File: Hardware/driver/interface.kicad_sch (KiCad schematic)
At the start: 45 parts, among them J201 Conn_02x10_Odd_Even, M201 Fan_4pin, Q201 MMBT3904, Q202 PN2222A, U201 AT24CS32-SSHM, U202 ADUM1250, U203 FODM214, U204 EMC2101-R, U205 NCP716BCSN330T1G

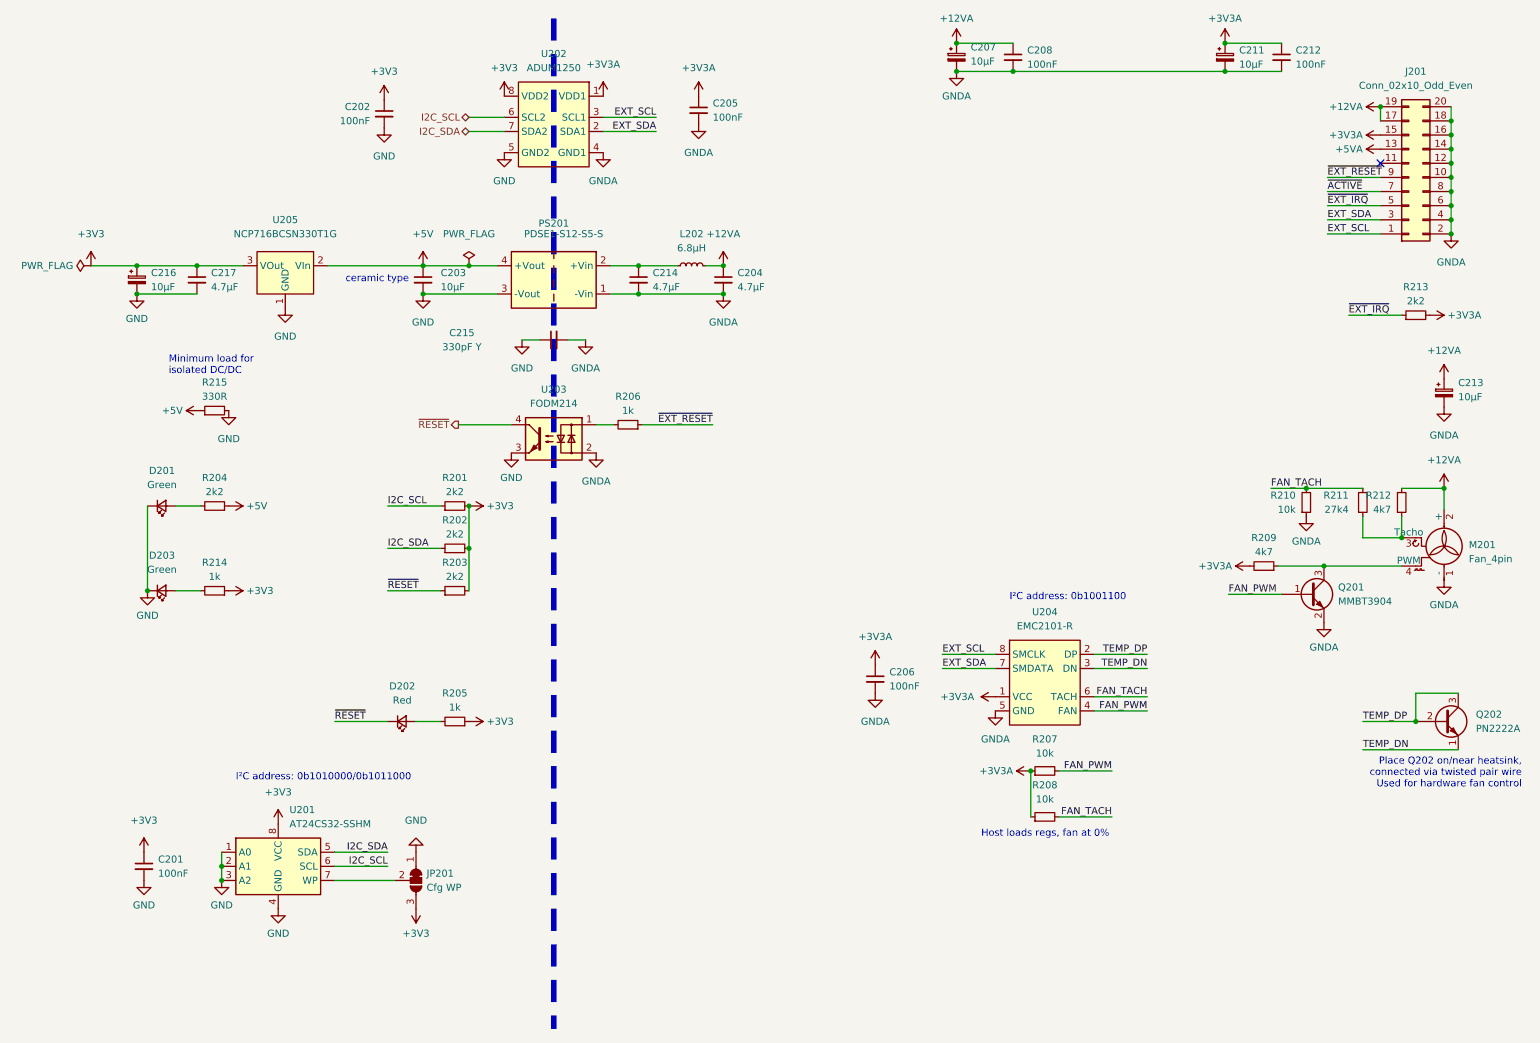
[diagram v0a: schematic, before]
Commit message: External trigger input
- Added a basic Schmitt-trigger based external trigger input. There's a
  basic pulse shaping circuit attached to it, before its fed into the
  buffer, and then off to the main board to use as an interrupt line to
  control the system mode.
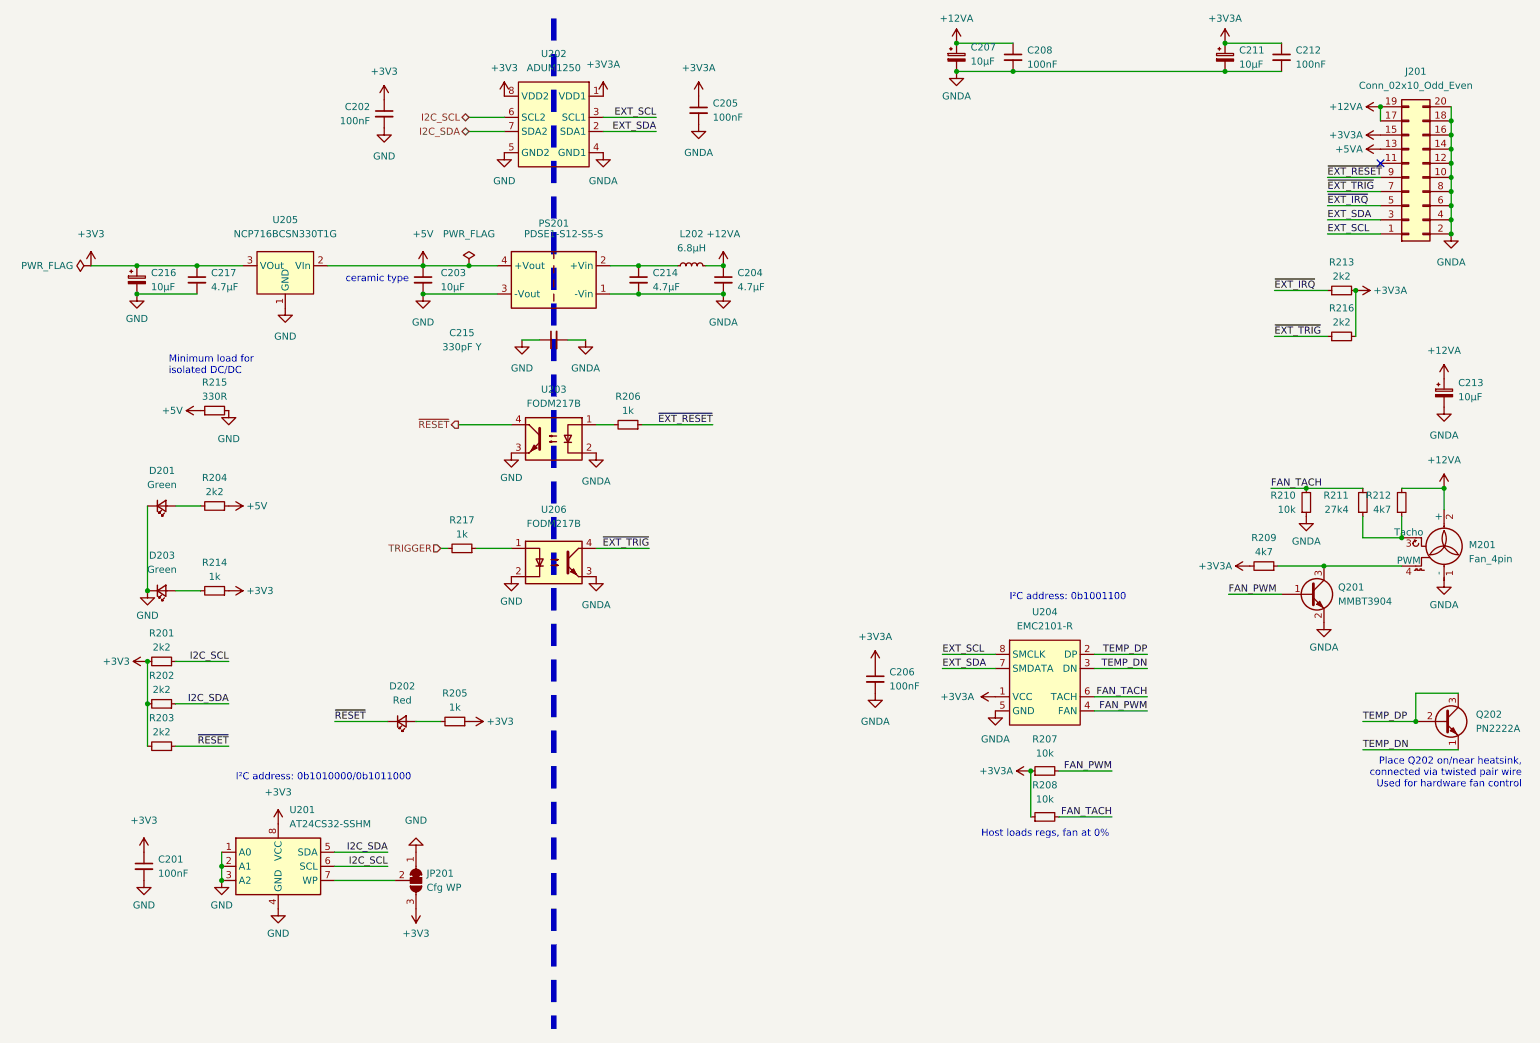
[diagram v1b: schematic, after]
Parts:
- added R216: 2k2, Resistor_SMD:R_0805_2012Metric_Pad1.20x1.40mm_HandSolder, symbol Device:R_Small
- added R217: 1k, Resistor_SMD:R_0805_2012Metric_Pad1.20x1.40mm_HandSolder, symbol Device:R_Small
- added U206: FODM217B, Package_SO:SOP-4_4.4x2.6mm_P1.27mm, symbol Isolator:FODM217B
- U203: value FODM214 -> FODM217B; symbol Isolator:FODM214 -> Isolator:FODM217B; MPN (none) -> FODM217B
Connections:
- net +3V3A: now also R216.2
- net GND: now also U206.2
- net GNDA: now also U206.3
- net ~{ACTIVE} renamed ~{EXT_TRIG}
- net ~{EXT_TRIG}: now also R216.1, U206.4
- new net: R217.1, U206.1
- new net TRIGGER: R217.2
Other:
- moved on the sheet: R201, R202, R203, R213

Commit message: Start work on remote VSense; driver board tweaks
- Use the DAC reference as the positive end of the null adjustment
  trimmers, rather than the +3V3 supply; this should make the adjustment
  actually useful and persistent rather than relying on the relationship
  between the 3V3 rail and the DAC's internal reference.

- Moved the 1Wire controller slightly to allow relocating the zero
  offset trimmer for the first channel

- Start work on remote VSense

  This works by selecting between either voltage sensing at the source
  terminals, or an external sense input connected to another set of
  terminals. These are switched by a latching relay (as to provide
  satisfying clicky noises) and then go into an op amp working as a
  differential amplifier; it performs a 50:1 gain (obviating the need
  for resistor dividers, and providing greater accuracy) and that then
  goes into the measurement ADC as normal.

  We have to still figure out how to drive the relay (probably just an
  IO expander?) and place those components on the board.
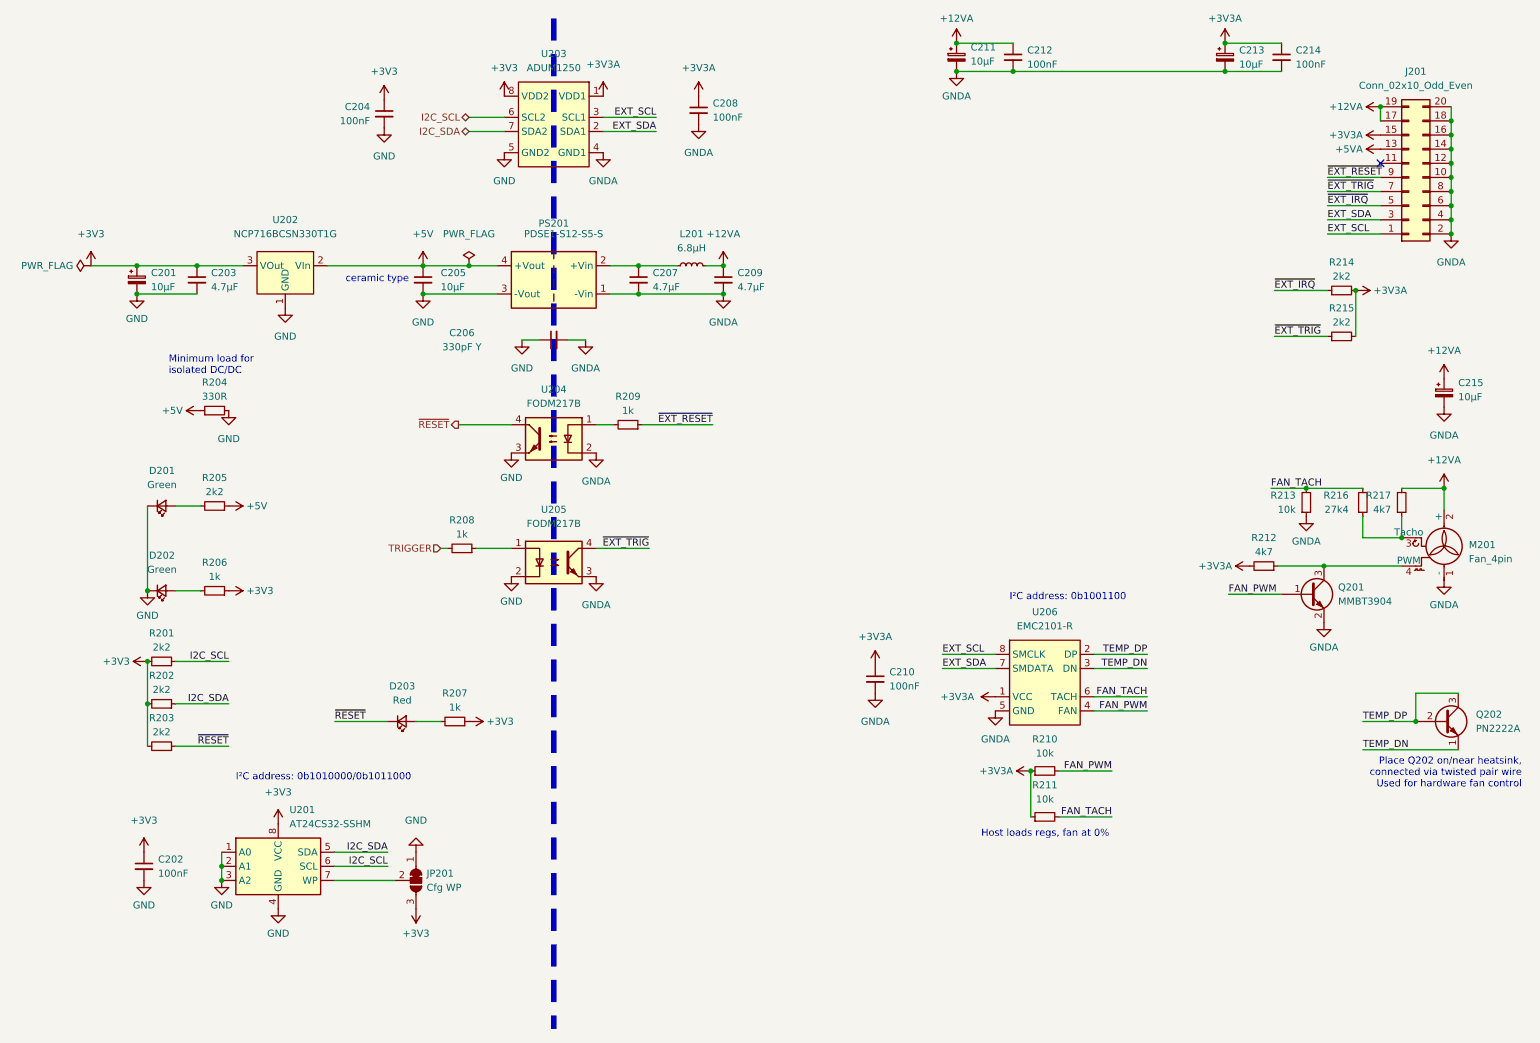
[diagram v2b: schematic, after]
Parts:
- renumbered C216 to C201, C201 to C202, C217 to C203, C202 to C204, C203 to C205, C215 to C206, C214 to C207, C205 to C208, C204 to C209, C206 to C210, C207 to C211, C208 to C212, C211 to C213, C212 to C214, C213 to C215, D203 to D202, D202 to D203, L202 to L201, R215 to R204, R204 to R205, R214 to R206, R205 to R207, R217 to R208, R206 to R209, R207 to R210, R208 to R211, R209 to R212, R210 to R213, R213 to R214, R216 to R215, R211 to R216, R212 to R217, U205 to U202, U202 to U203, U203 to U204, U206 to U205, U204 to U206

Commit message: Begin rev2 of driver board
- Improve the power side of things to provide +15V, +12V, +5V, +3V3, and
  -5V on the isolated side of the driver board. This is needed so that
  we can have the +12V for driving opamps with wider swing for the
  drive MOSFETs; these will not turn on with 3V3 as in the original rev1
  design so new driver op amps (U302, U306) need to be chosen
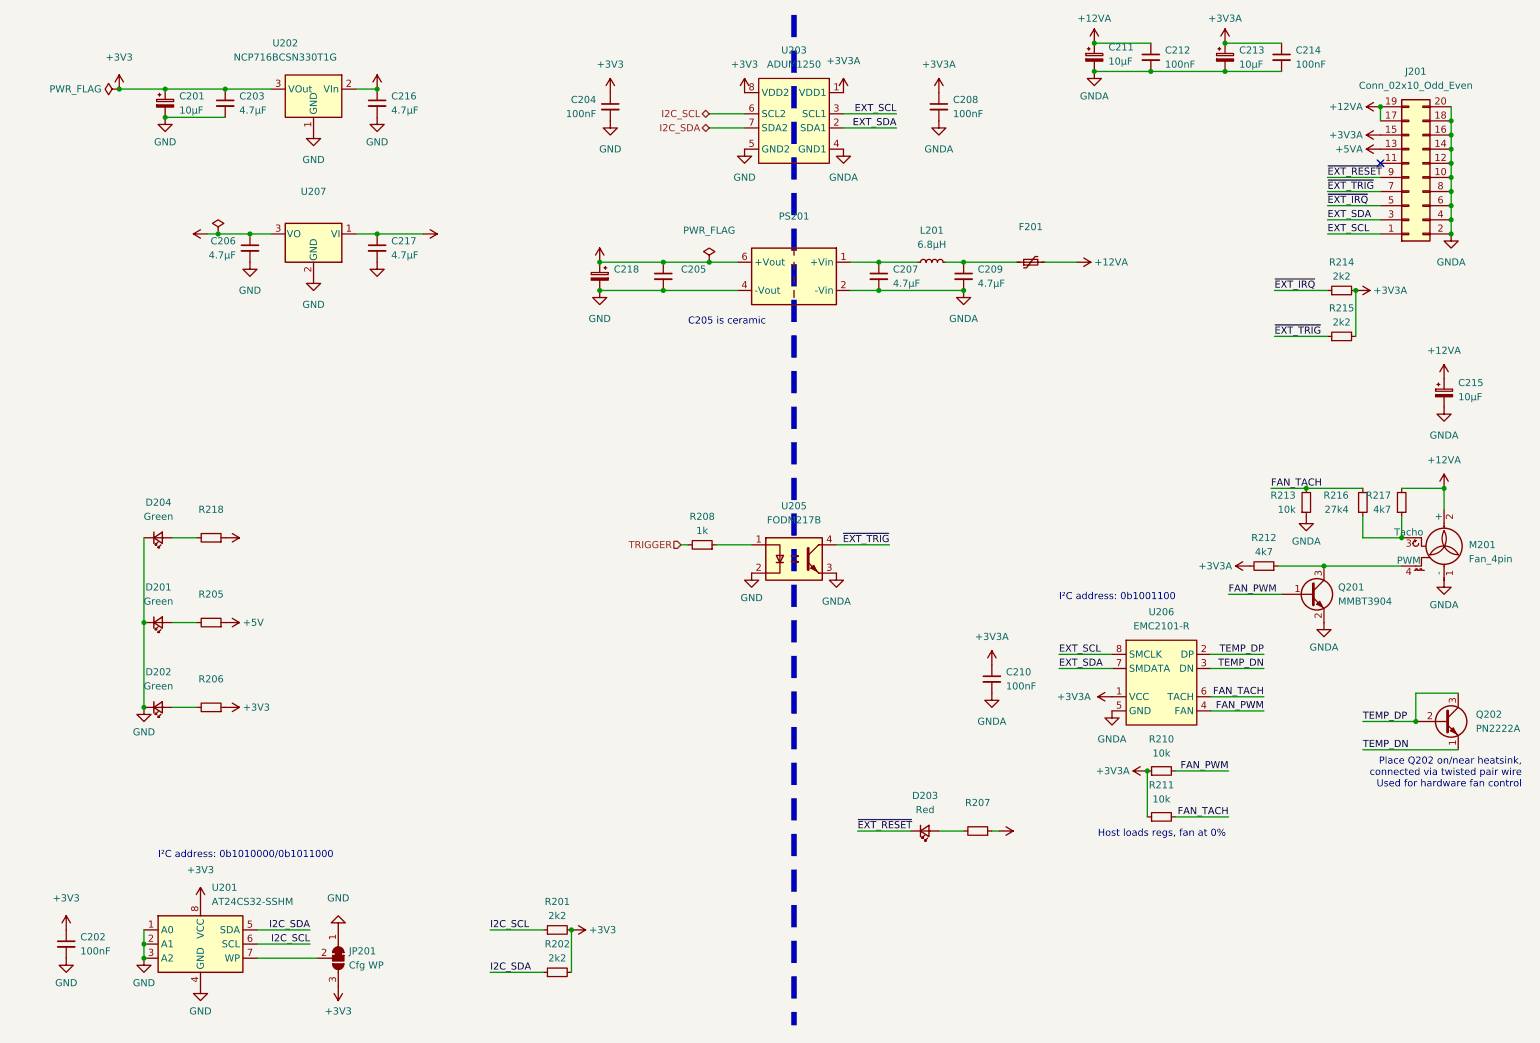
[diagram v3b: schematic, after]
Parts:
- removed PS201: PDSE1-S12-S5-S, programmable-load:CONV_PDSE1-S12-S3-S, symbol programmable-load:PDSE1-S12-S3-S
- removed R203: 2k2, Resistor_SMD:R_0805_2012Metric_Pad1.20x1.40mm_HandSolder, symbol Device:R_Small
- removed R204: 330R, Resistor_SMD:R_0805_2012Metric_Pad1.20x1.40mm_HandSolder, symbol Device:R_Small
- removed R209: 1k, Resistor_SMD:R_0805_2012Metric_Pad1.20x1.40mm_HandSolder, symbol Device:R_Small
- removed U204: FODM217B, Package_SO:SOP-4_4.4x2.6mm_P1.27mm, symbol Isolator:FODM217B
- added C216, C217: 4.7µF, Capacitor_SMD:C_0805_2012Metric_Pad1.18x1.45mm_HandSolder, symbol Device:C_Small
- added C218: (no value), symbol Device:C_Polarized_Small
- added D204: Green, LED_SMD:LED_0805_2012Metric_Pad1.15x1.40mm_HandSolder, symbol Device:LED_Small
- added F201: (no value), symbol Device:Polyfuse_Small
- added PS201: (no value), symbol programmable-load:PCN2-S12-S15-S
- added R218: (no value), symbol Device:R_Small
- added U207: (no value), symbol Regulator_Linear:MCP1703A-5002_SOT223
- C205: value 10µF -> (none); footprint Capacitor_SMD:C_0805_2012Metric_Pad1.18x1.45mm_HandSolder -> (none); MPN CL21A106KPFNNNF -> TMK212BBJ106MG-T
- C206: value 330pF Y -> 4.7µF; footprint Capacitor_THT:C_Disc_D7.5mm_W2.5mm_P5.00mm -> Capacitor_SMD:C_0805_2012Metric_Pad1.18x1.45mm_HandSolder; MPN F331K29Y5RP6UK5R -> CL21A475KAQNNNF
- R205: value 2k2 -> (none); footprint Resistor_SMD:R_0805_2012Metric_Pad1.20x1.40mm_HandSolder -> (none); MPN (none) -> RMC1/10-222JTP
- R206, R207: value 1k -> (none); footprint Resistor_SMD:R_0805_2012Metric_Pad1.20x1.40mm_HandSolder -> (none); MPN (none) -> CR0805-JW-102ELF
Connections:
- net ~{RESET} is gone; now on net ~{EXT_RESET}: D203.1 (K)
- net +12VA: now also F201.2; no longer C209.1, L201.2
- net +3V3: no longer R207.1
- net +3V3A: now also R207.1
- net +5V: now also C206.1, C216.1, U207.3 (VO); no longer C205.1
- net GND: now also C206.2, C216.2, C217.2, C218.2, D204.1 (K), PS201.4 (-Vout), U207.2 (GND); no longer C206.1
- net GNDA: now also PS201.2 (-Vin); no longer C206.2
- net at C207.1, L201.1: now also PS201.1 (+Vin)
- new net: C209.1, F201.1, L201.2
- new net: D204.2 (A), R218.2
- new net +15V: C205.1, C217.1, C218.1, PS201.6 (+Vout), R218.1, U207.1 (VI)
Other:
- note added: "C205 is ceramic"
- note removed: "Minimum load for isolated DC/DC"
- note removed: "ceramic type"
- moved on the sheet: C201, C202, C203, C204, C205, C207, C208, C209, C210, C211, C212, D201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

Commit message: More rev 2 driver board work
- Updated power supply section with linear regulators for the +12V and
  +5V rails

- Replaced op amps for driving the MOSFETs with different ones, and
  updated them so that they actually run off the 12V rail instead of the
  3V3 rail.
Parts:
- added C219: 100nF, Capacitor_SMD:C_0805_2012Metric_Pad1.18x1.45mm_HandSolder, symbol Device:C_Small
- added C220, C221: 4.7µF, Capacitor_SMD:C_0805_2012Metric_Pad1.18x1.45mm_HandSolder, symbol Device:C_Small
- added D205, D206: Green, LED_SMD:LED_0805_2012Metric_Pad1.15x1.40mm_HandSolder, symbol Device:LED_Small
- added R203: 2k2, Resistor_SMD:R_0805_2012Metric_Pad1.20x1.40mm_HandSolder, symbol Device:R_Small
- added R204: (no value), symbol Device:R_Small
- added U204: (no value), symbol Regulator_Linear:MCP1804x-C002xMB
- C205: value (none) -> 10µF; footprint (none) -> Capacitor_SMD:C_0805_2012Metric_Pad1.18x1.45mm_HandSolder
- C218: value (none) -> 47µF; footprint (none) -> Capacitor_THT:CP_Radial_D6.3mm_P2.50mm
- F201: value (none) -> 350mA; footprint (none) -> Fuse:Fuse_1210_3225Metric_Pad1.42x2.65mm_HandSolder
- PS201: value (none) -> PCN2-S12-S15-S; footprint (none) -> programmable-load:CONV_PCN2-S12-S15-S
- R205: value (none) -> 2k2; footprint (none) -> Resistor_SMD:R_0805_2012Metric_Pad1.20x1.40mm_HandSolder
- R206, R207: value (none) -> 1k; footprint (none) -> Resistor_SMD:R_0805_2012Metric_Pad1.20x1.40mm_HandSolder
- R218: value (none) -> 7k5; footprint (none) -> Resistor_SMD:R_0805_2012Metric_Pad1.20x1.40mm_HandSolder
- U207: value (none) -> MCP1703AT-5002E/DB; footprint (none) -> Package_TO_SOT_SMD:SOT-223-3_TabPin2
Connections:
- net +15V: now also C221.1, U204.1 (OUT)
- net GND: now also C219.2, C220.2, C221.2, D205.2 (A), D206.1 (K), U204.2 (GND)
- new net: D205.1 (K), R203.2
- new net: D206.2 (A), R204.2
- new net +12V: C219.1, C220.1, R204.1, U204.3 (IN)
- new net -5V: R203.1
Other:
- moved on the sheet: C201, C203, C206, C216, C217, D201, D202, D204, R205, R206, R218, U202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

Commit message: More work on rev2 driver board
- Tweaked the board layout for the load driver some more, primarily
  relating to power and friends

- Fixed footprint of fan connector on driver board (to properly have the
  mechanical mounting hole)

- Manufacturability/solderability tweaks for a few other footprints
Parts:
- removed C219: 100nF, Capacitor_SMD:C_0805_2012Metric_Pad1.18x1.45mm_HandSolder, symbol Device:C_Small
- removed U202: NCP716BCSN330T1G, Package_SO:TSOP-5_1.65x3.05mm_P0.95mm, symbol programmable-load:NCP716BC
- added U202: (no value), symbol Regulator_Linear:MIC5366-3.3YC5
- M201: value Fan_4pin -> (none); footprint Connector_Molex:Molex_KK-254_AE-6410-04A_1x04_P2.54mm_Vertical -> (none)
- R204: value (none) -> 4k99; footprint (none) -> Resistor_SMD:R_0805_2012Metric_Pad1.20x1.40mm_HandSolder
- U204: value (none) -> MCP1804x-C002xMB; footprint (none) -> Package_TO_SOT_SMD:SOT-89-3
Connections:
- net +12V: now also U204.1 (OUT); no longer U204.3 (IN)
- net +12VA: now also R212.2
- net +15V: now also U204.3 (IN); no longer U204.1 (OUT)
- net +3V3: now also U202.5 (VOUT)
- net +3V3A: no longer R212.2
- net +5V: now also U202.1 (VIN), U202.3 (EN)
- net GND: now also U202.2 (GND)
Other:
- moved on the sheet: C216
